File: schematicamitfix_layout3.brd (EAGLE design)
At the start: 28 x 47 mm, 39 parts, among them J1 FTDI_DEVICE, M1 WIRELESS-NRF24L01, U1 ATMEGA328P_TQFP, U2 GY-521MPU6050, U3 MAX1595EUA33+, Y1 8MHz

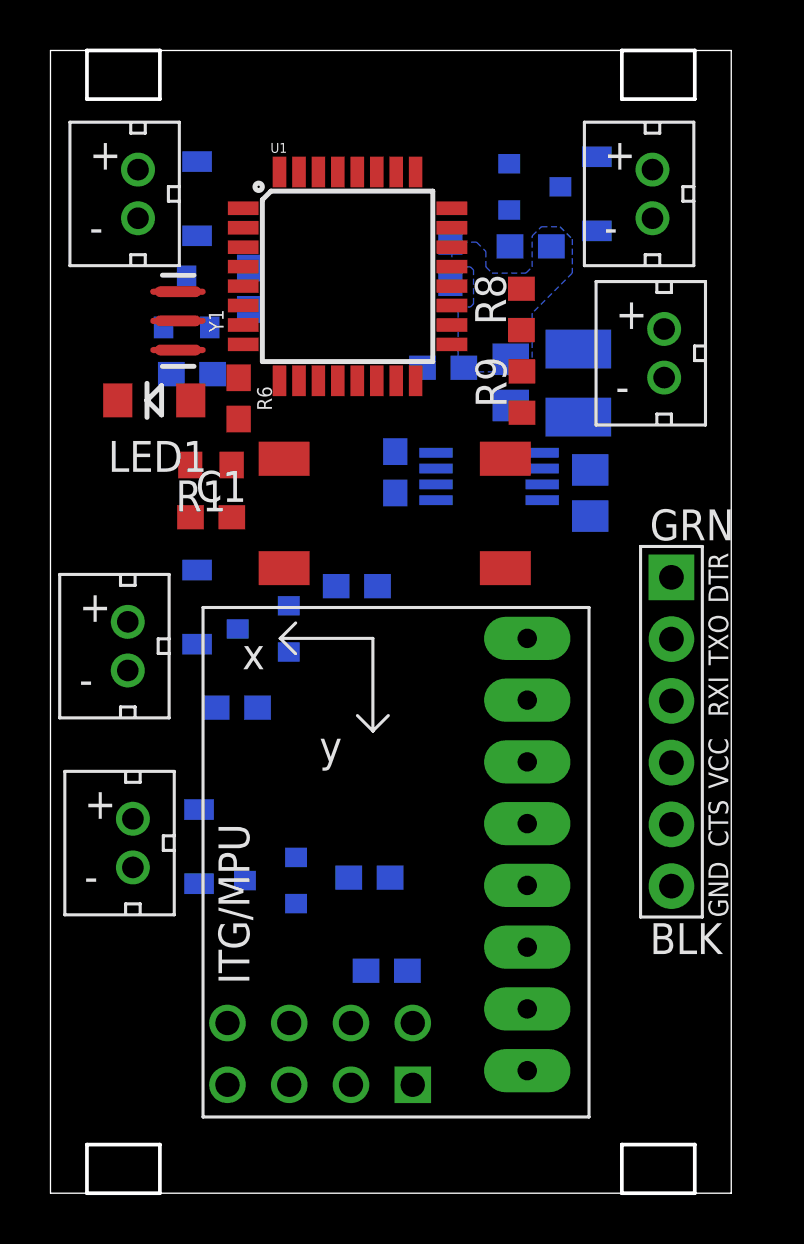
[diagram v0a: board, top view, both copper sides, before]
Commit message: Added layout3 (Plane Layout), and routed most of the board.  Outstanding issues remain.
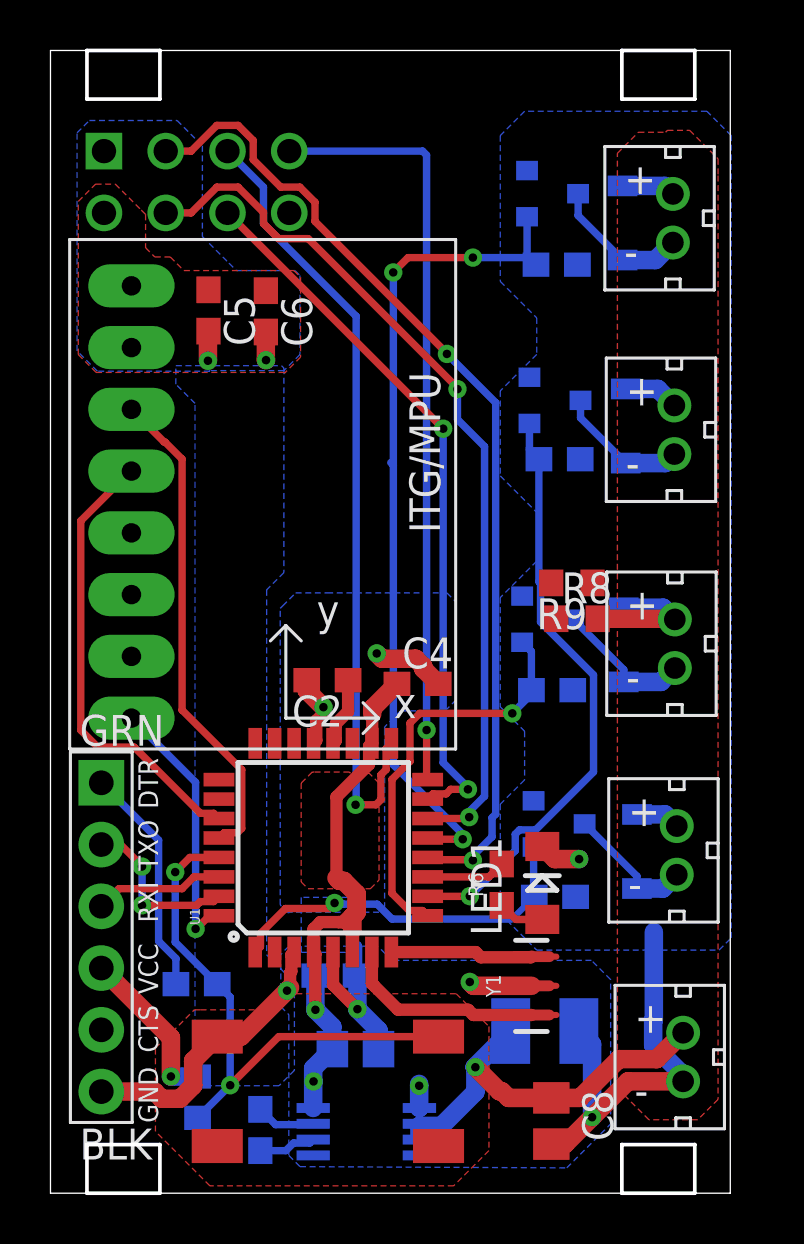
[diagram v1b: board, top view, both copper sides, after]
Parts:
- moved Y1 31.0 mm to (19.8, 8.53), turned to 90 degrees
- moved U$19 29.0 mm to (26.0, 5.60)
- moved C3 28.5 mm to (11.7, 8.95), turned to 180 degrees
- moved C12 28.2 mm to (12.5, 5.93), turned to 180 degrees
- moved C5 28.1 mm to (6.50, 36.3), flipped to the top, turned to 270 degrees
- moved U$3 28.0 mm to (25.7, 31.4)
- moved C7 27.6 mm to (8.63, 2.60)
- moved U3 27.4 mm to (13.0, 2.53)
- moved U$6 27.1 mm to (24.1, 14.0)
- moved U$7 27.0 mm to (25.8, 14.1)
- moved R2 26.8 mm to (20.8, 12.2)
- moved C13 26.7 mm to (20.3, 6.67), turned to 0 degrees
- moved U$12 26.2 mm to (20.9, 15.2)
- moved R1 26.0 mm to (6.05, 3.95), flipped to the bottom, turned to 90 degrees
- moved C8 25.9 mm to (20.6, 2.97), flipped to the top
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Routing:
- net GND: track 0.00 -> 49.1 mm, vias 0 -> 9
- net NRF_CE: track 0.00 -> 40.8 mm, vias 0 -> 2
- net NRF_CSN: track 0.00 -> 36.3 mm, vias 0 -> 2
- net PWM4: track 0.00 -> 34.7 mm, vias 0 -> 3
- net VCC: track 0.00 -> 34.1 mm, vias 0 -> 4
- net NRF_SCK: track 0.00 -> 32.7 mm, vias 0 -> 1
- net NRF_MISO: track 0.00 -> 31.5 mm, vias 0 -> 1
- net NRF_MOSI: track 0.00 -> 29.6 mm, vias 0 -> 2
- net VIN: track 0.00 -> 28.5 mm, vias 0 -> 1
- net PWM2: track 0.00 -> 24.8 mm, vias 0 -> 1
- net N$1: track 0.00 -> 23.0 mm, vias 0 -> 2
- net IMU_SCL: track 0.00 -> 20.2 mm
- net IMU_SDA: track 0.00 -> 18.7 mm
- net PWM3: track 0.00 -> 16.9 mm, vias 0 -> 1
- net PWM1: track 0.00 -> 15.3 mm, vias 0 -> 1
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- added copper zone on layer 16, net GND
- added copper zone on layer 1, net VCC
- added copper zone on layer 1, net VIN
- removed copper zone on layer 16, net N$3

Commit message: Revision #2 to send
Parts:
- moved R9 10.2 mm to (11.4, 23.4), turned to 0 degrees
- moved J1 2.44 mm to (3.04, 12.8)
- moved U2 2.35 mm to (12.2, 30.8)
- moved M1 2.30 mm to (10.2, 31.8)
- moved U$19 2.00 mm to (26.0, 7.60)
- moved R1 1.36 mm to (5.85, 2.60)
- moved U$15 1.00 mm to (25.6, 39.1)
- moved U$8 0.30 mm to (20.7, 23.6)
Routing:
- net AIN: track 0.04 -> 17.6 mm
- net FTDI_DTR: track 9.55 -> 15.6 mm
- net FTDI_TX: track 7.22 -> 13.1 mm, vias 2 -> 1
- net VCC: track 34.1 -> 28.5 mm
- net IMU_INT: track 11.0 -> 15.5 mm
- net NRF_MOSI: track 29.6 -> 33.3 mm, vias 2 -> 1
- net IMU_SCL: track 20.2 -> 22.6 mm
- net NRF_SCK: track 32.7 -> 35.1 mm
- net PWM2: track 24.8 -> 22.6 mm
- net NRF_CSN: track 36.3 -> 34.7 mm
- net FTDI_RX: track 5.34 -> 6.54 mm, vias 0 -> 1
- net PWM3: track 16.9 -> 18.1 mm
- net N$1: track 23.0 -> 24.2 mm
- net NRF_MISO: track 31.5 -> 30.5 mm
- net VIN: track 28.5 -> 29.2 mm
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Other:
- outline, holes or cut-outs redrawn
